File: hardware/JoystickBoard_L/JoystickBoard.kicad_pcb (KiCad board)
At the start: 2 copper layers, 8 parts, among them J1 RJHSE-3380, J2 S1, J3 S2, J4 JoyX, J5 JoyY, J6 LED1, J7 LED2

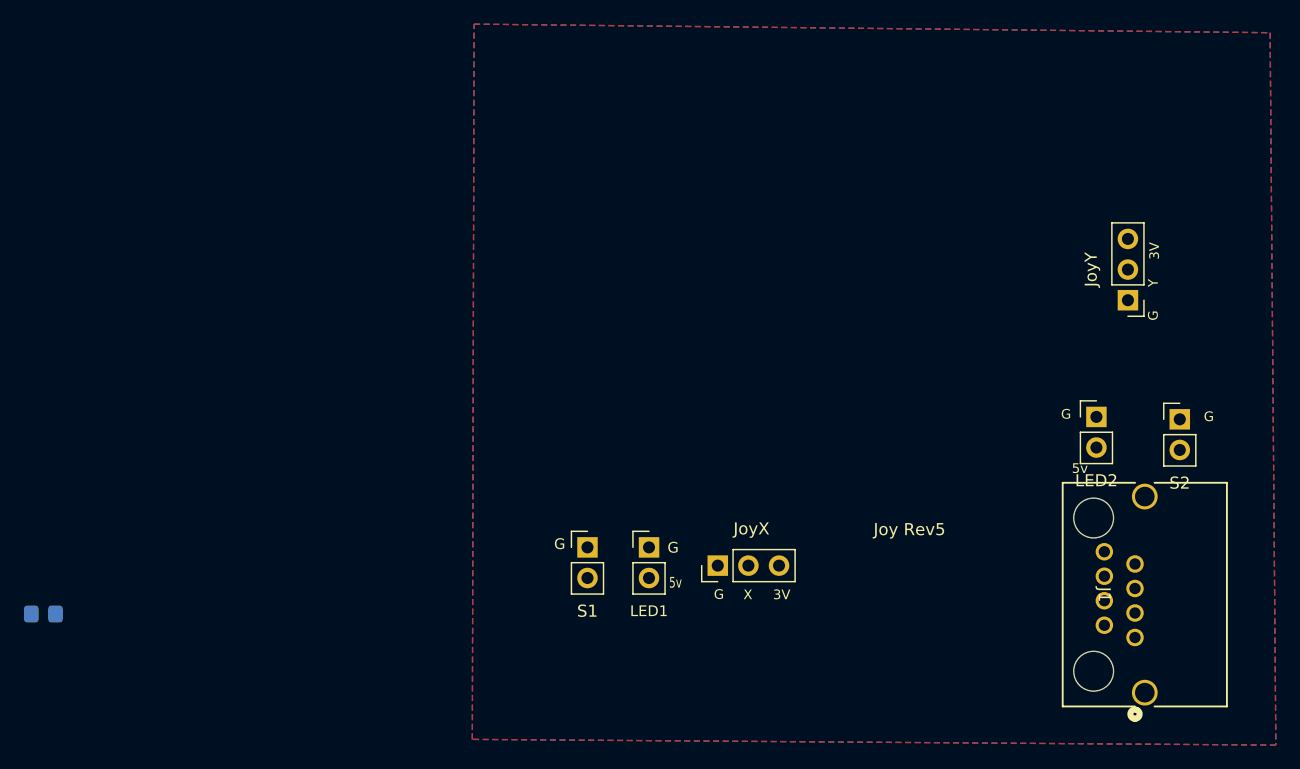
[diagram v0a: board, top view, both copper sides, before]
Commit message: Updates to Joystick_L
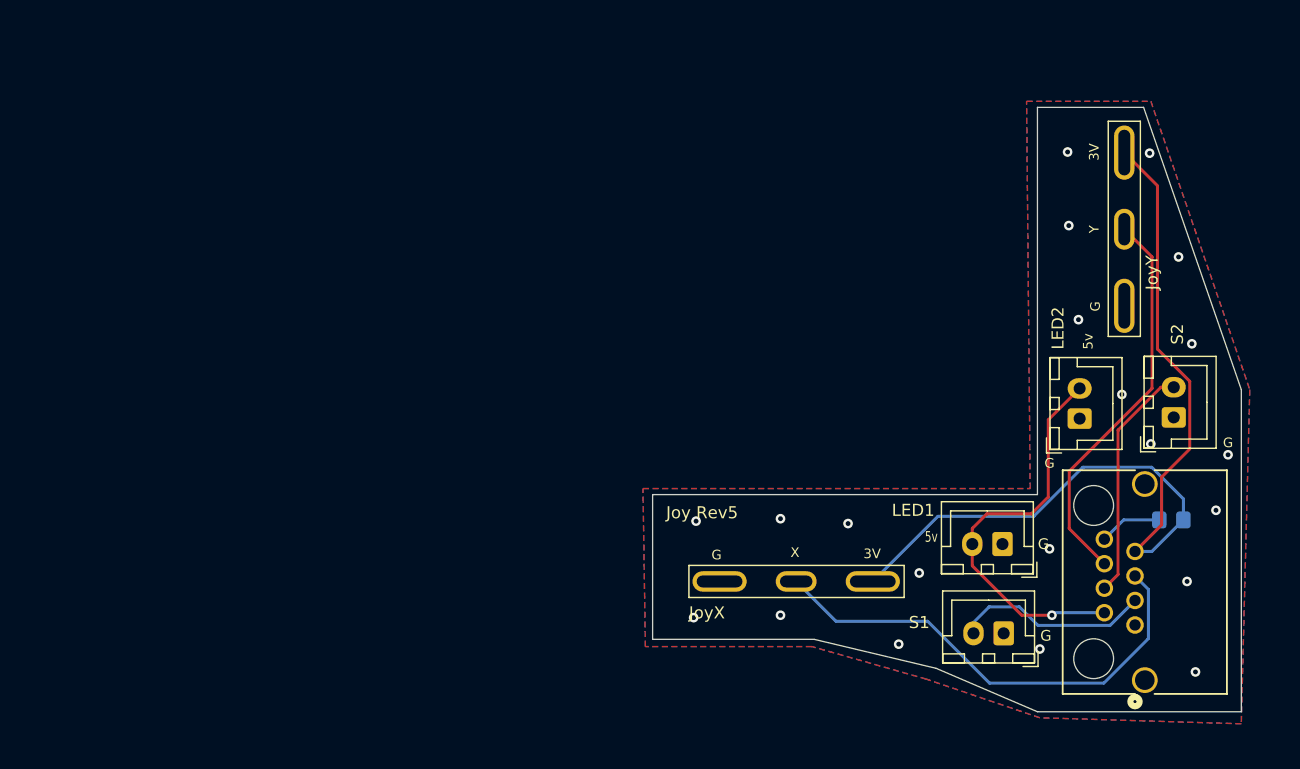
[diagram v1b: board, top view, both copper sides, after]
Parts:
- J2, J3, J6, J7: footprint Connector_PinHeader_2.54mm:PinHeader_1x02_P2.54mm_Vertical -> Connector_JST:JST_XH_B2B-XH-A_1x02_P2.50mm_Vertical
- J4, J5: footprint Connector_PinHeader_2.54mm:PinHeader_1x03_P2.54mm_Vertical -> Useful Modifications:Analog_joystick_pot
- moved R1 93.8 mm to (190.0, 97.2), turned to 0 degrees
- moved J2 35.2 mm to (176.1, 106.6), turned to 180 degrees
- moved J6 29.3 mm to (176.0, 99.2), turned to 180 degrees
- moved J4 6.63 mm to (158.9, 102.3)
- moved J5 5.89 mm to (186.1, 73.1)
- moved J7 1.40 mm to (182.4, 88.8), turned to 90 degrees
- moved J1 1.04 mm to (187.0, 105.9)
- moved J3 0.52 mm to (190.2, 88.7), turned to 90 degrees
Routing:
- net +3.3V: track 0.00 -> 74.8 mm
- net JoystickX: track 0.00 -> 39.9 mm
- net +5V: track 0.00 -> 33.3 mm, vias 0 -> 1
- net JoystickY: track 0.00 -> 32.7 mm
- net Sound2: track 0.00 -> 19.7 mm
- net Sound1: track 0.00 -> 16.3 mm
- net Net-(J1-Pad8): track 0.00 -> 5.21 mm
- net GND: vias 0 -> 21
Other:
- board outline added: 48.8 x 50.1 mm

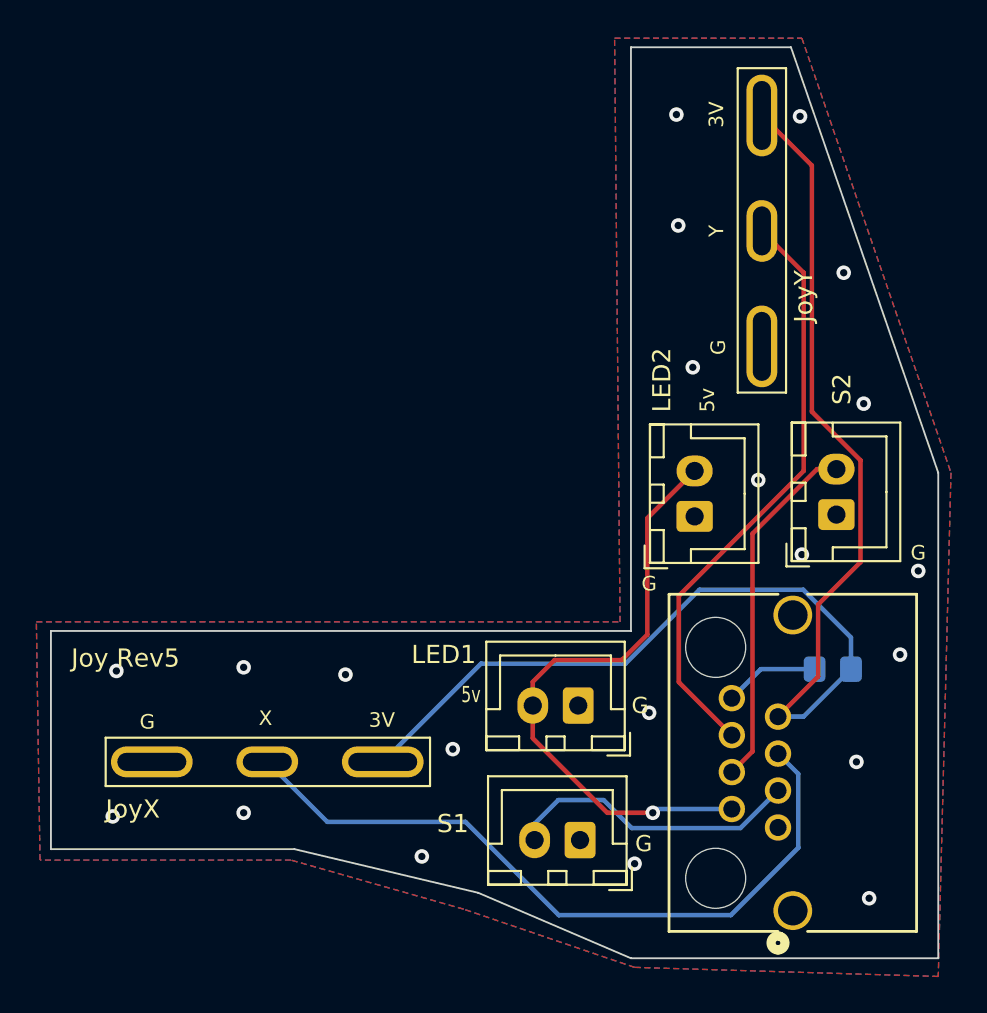
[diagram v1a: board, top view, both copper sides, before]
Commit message: reworking L-shaped analog joystick PCB
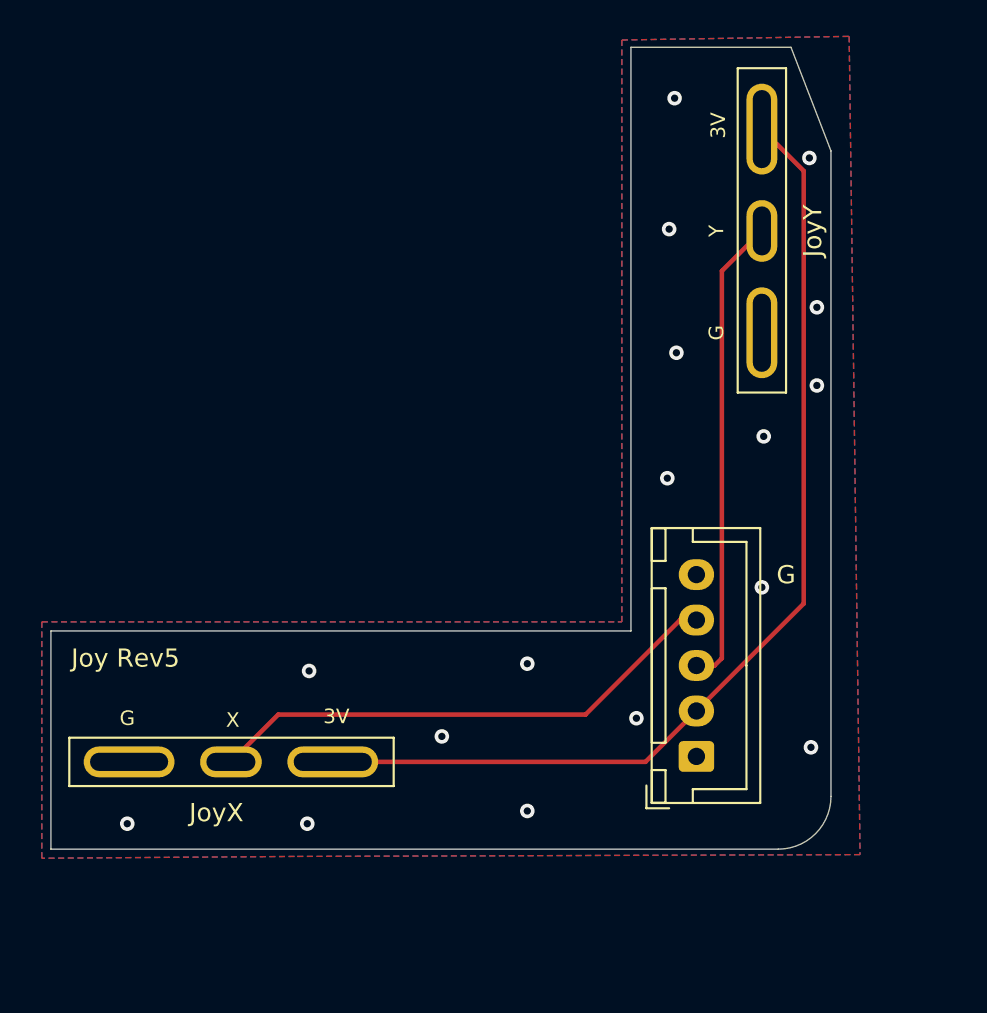
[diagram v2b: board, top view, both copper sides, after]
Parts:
- removed J2: S1, Connector_JST:JST_XH_B2B-XH-A_1x02_P2.50mm_Vertical
- removed J3: S2, Connector_JST:JST_XH_B2B-XH-A_1x02_P2.50mm_Vertical
- removed J6: LED1, Connector_JST:JST_XH_B2B-XH-A_1x02_P2.50mm_Vertical
- removed J7: LED2, Connector_JST:JST_XH_B2B-XH-A_1x02_P2.50mm_Vertical
- removed R1: 10K, Resistor_SMD:R_0805_2012Metric_Pad1.20x1.40mm_HandSolder
- J1: value RJHSE-3380 -> Conn_01x05_Pin; footprint Useful Modifications:CONN_RJHSE-3380_AMP -> Connector_JST:JST_XH_B5B-XH-A_1x05_P2.50mm_Vertical
- moved J1 5.95 mm to (182.5, 102.0), turned to 90 degrees
- moved J4 2.00 mm to (156.9, 102.3)
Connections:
- J1 pad 1: GND -> unconnected-(J1-Pin_1-Pad1)
- J1 pad 2: +5V -> +3.3V
- J1 pad 3: Sound1 -> JoystickY
- J1 pad 4: Sound2 -> JoystickX
- J1 pad 5: JoystickX -> GND
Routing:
- net +5V: track 33.3 -> 0.00 mm, vias 1 -> 0
- net Sound2: track 19.7 -> 0.00 mm
- net +3.3V: track 74.8 -> 56.6 mm
- net Sound1: track 16.3 -> 0.00 mm
- net JoystickX: track 39.9 -> 28.8 mm
- net JoystickY: track 32.7 -> 26.0 mm
- net Net-(J1-Pad8): track 5.21 -> 0.00 mm
- net GND: vias 21 -> 17
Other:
- board size 48.8 x 50.1 mm -> 42.9 x 44.1 mm
- board text removed: "5V"
- board text removed: "5v"
- board text removed: "Active"
- board text removed: "Gnd"
- board text removed: "S1"
- board text removed: "S2"
